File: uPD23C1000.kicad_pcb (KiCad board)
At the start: 2 copper layers, 16.5 x 34.3 mm, 9 parts, among them J1 uPD23C1000, J2 Conn_1x2, J3 Conn_1x3, U1 29F010 TSOP-32 20mm, U2 29F010 sTSOP-32 14mm, U3 29F010 PLCC-32 7x9

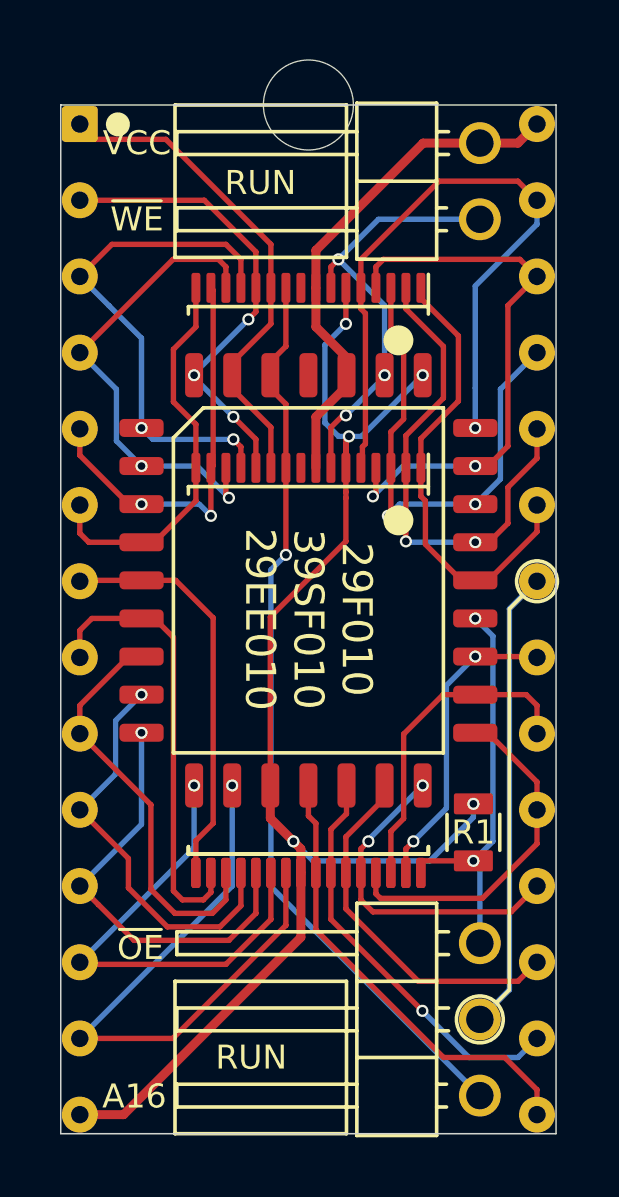
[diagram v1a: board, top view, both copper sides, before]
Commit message: add FlashROM_100_tsop
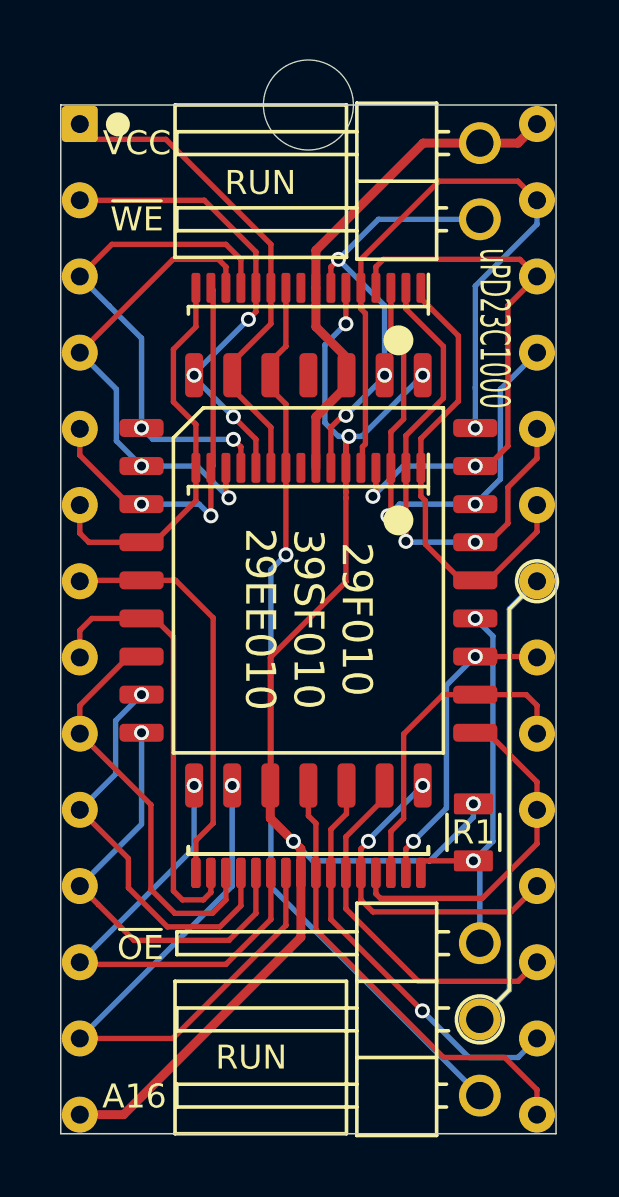
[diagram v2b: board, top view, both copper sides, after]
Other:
- net class Default: clearance 0.1524 -> 0.16; via_dia 0.4064 -> 0.5; via_drill 0.254 -> 0.3
- rule trace_clearance: 0.1524 -> 0.16
- rule via_min_drill: 0.254 -> 0.3
- rule via_min_size: 0.4064 -> 0.5
- board text added: "uPD23C1000"
